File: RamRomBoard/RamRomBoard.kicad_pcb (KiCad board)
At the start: 2 copper layers, 100 x 100 mm, 74 parts, among them J1 BUS, J10 ., J13 ., J2 BUS, J3 Spare, J4 Spare, J5 Screw_Terminal_01x02, J6 USB_B_Micro, J7 STM32F401, J8 Dual LED Socket, J9 JTAG, SW1 033TBVSA, U1 74LVC125, U10 74AHC1G14, U11 IS61WV102416, U12 IS61WV10248EDBLL, U13 74LVC595, U14 74LVC595, U15 SN74LVC245ANSR, U16 SN74LVC245ANSR, U17 74LVC595, U18 74HC165, U19 SN74LVC245ANSR, U2 AZ1117-3.3, U3 74LVC08AD, U4 DS1085, U5 74LVC1G32, U6 74AHC1G14, U7 74HC590, U8 74HC590, U9 74HC590

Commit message: Readme update
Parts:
- J5: footprint Connector_Phoenix_MC:PhoenixContact_MCV_1,5_2-G-3.81_1x02_P3.81mm_Vertical -> TerminalBlock_RND:TerminalBlock_RND_205-00012_1x02_P5.00mm_Horizontal
- moved J5 0.67 mm to (61.2, 54.6)
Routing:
- net GND: track 979.5 -> 978.5 mm

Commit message: cpld examples update
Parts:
- U11: value IS61WV102416 -> IS61WV102416FBLL1T2
- U12: value IS61WV10248EDBLL -> IS61WV10248EDBLL-10TL
- U2: footprint Package_TO_SOT_SMD:SOT-89-3_Handsoldering -> Package_TO_SOT_SMD:SOT-223-3_TabPin2
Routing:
- net /A10: track 70.9 -> 68.1 mm
- net /A11: track 67.0 -> 64.9 mm
- net /A19: track 97.2 -> 95.2 mm
- net /A8: track 87.8 -> 85.9 mm
- net /A9: track 74.8 -> 73.4 mm
- net +5V: track 280.2 -> 278.9 mm
- net /A7: track 81.2 -> 80.2 mm
- net +3V3: track 716.5 -> 717.4 mm
- net /A14: track 64.5 -> 65.3 mm
- net /A6: track 87.9 -> 87.2 mm
- net /CPR: track 85.6 -> 85.0 mm
- net /A12: track 68.0 -> 67.5 mm

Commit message: New XC9572 Example
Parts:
- removed J10, J13: ., Connector_PinHeader_2.00mm:PinHeader_1x01_P2.00mm_Vertical
- added TP10: ., Connector_PinHeader_1.00mm:PinHeader_1x01_P1.00mm_Vertical, F.Cu at (80.3, 121.7)
- added TP11: ., Connector_PinHeader_1.00mm:PinHeader_1x01_P1.00mm_Vertical, F.Cu at (80.4, 113.9)
- added TP12: ., Connector_PinHeader_1.00mm:PinHeader_1x01_P1.00mm_Vertical, F.Cu at (58.4, 113.9)
- added TP13: ., Connector_PinHeader_1.00mm:PinHeader_1x01_P1.00mm_Vertical, F.Cu at (58.4, 119.1)
- added TP14: ., Connector_PinHeader_1.00mm:PinHeader_1x01_P1.00mm_Vertical, F.Cu at (58.5, 93.7)
- added TP15: ., Connector_PinHeader_1.00mm:PinHeader_1x01_P1.00mm_Vertical, F.Cu at (58.4, 103.9)
- R1: value 1k -> 560E
- moved REF** 83.6 mm to (62.2, 144.8), turned to 0 degrees
- moved REF** 76.3 mm to (76.8, 144.1), turned to 0 degrees
- moved C16 9.47 mm to (143.9, 121.3), turned to 0 degrees
- moved RN3 7.59 mm to (136.8, 131.6)
- moved RN4 7.59 mm to (138.0, 135.0)
- moved C13 6.30 mm to (131.2, 101.2)
- moved U10 6.30 mm to (116.5, 112.4)
- moved U15 6.30 mm to (132.0, 123.6)
- moved U16 6.30 mm to (118.7, 123.6)
- moved C10 6.30 mm to (110.1, 113.6)
- moved U13 6.30 mm to (130.7, 113.5)
- moved U14 6.30 mm to (117.5, 113.6)
- moved U11 6.21 mm to (131.8, 103.0)
- moved C11 0.55 mm to (124.1, 90.2)
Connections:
- net /uSCL renamed /uSCK
- net /uSDA renamed /uMOSI
- net /~{uSCL} renamed /~{uSCK}
- J2 pad 10: /Bus/RES1 -> /~{CE_EXT4}
- J2 pad 11: /Bus/RES0 -> /~{CE_EXT7}
- J2 pad 12: /~{CE_EXT0} -> /~{CE_EXT6}
- J2 pad 13: /~{CE_EXT1} -> /~{CE_EXT9}
- J2 pad 14: /~{CE_EXT2} -> /~{CE_EXT8}
- J2 pad 15: /~{CE_EXT3} -> /~{CE_EXT11}
- J2 pad 16: /~{CE_EXT4} -> /~{CE_EXT10}
- J2 pad 17: /~{CE_EXT5} -> /~{CE_EXT13}
- J2 pad 18: /~{CE_EXT6} -> /~{CE_EXT12}
- J2 pad 19: /~{CE_EXT7} -> /Bus/RES4
- J2 pad 20: /~{CE_EXT8} -> /Bus/RES5
- J2 pad 21: /~{CE_EXT9} -> /Bus/RES2
- J2 pad 22: /~{CE_EXT10} -> /Bus/RES3
- J2 pad 23: /~{CE_EXT11} -> /Bus/RES0
- J2 pad 24: /~{CE_EXT12} -> /Bus/RES1
- J2 pad 25: /~{CE_EXT13} -> /CLK1
- J2 pad 5: /Bus/RES6 -> /~{CE_EXT1}
- J2 pad 6: /Bus/RES5 -> /~{CE_EXT0}
- J2 pad 7: /Bus/RES4 -> /~{CE_EXT3}
- J2 pad 8: /Bus/RES3 -> /~{CE_EXT2}
- J2 pad 9: /Bus/RES2 -> /~{CE_EXT5}
- J4 pad 10: /Bus/RES1 -> /~{CE_EXT4}
- J4 pad 11: /Bus/RES0 -> /~{CE_EXT7}
- J4 pad 12: /~{CE_EXT0} -> /~{CE_EXT6}
- J4 pad 13: /~{CE_EXT1} -> /~{CE_EXT9}
- J4 pad 14: /~{CE_EXT2} -> /~{CE_EXT8}
- J4 pad 15: /~{CE_EXT3} -> /~{CE_EXT11}
- J4 pad 16: /~{CE_EXT4} -> /~{CE_EXT10}
- J4 pad 17: /~{CE_EXT5} -> /~{CE_EXT13}
- J4 pad 18: /~{CE_EXT6} -> /~{CE_EXT12}
- J4 pad 19: /~{CE_EXT7} -> /Bus/RES4
- J4 pad 20: /~{CE_EXT8} -> /Bus/RES5
- J4 pad 21: /~{CE_EXT9} -> /Bus/RES2
- J4 pad 22: /~{CE_EXT10} -> /Bus/RES3
- J4 pad 23: /~{CE_EXT11} -> /Bus/RES0
- J4 pad 24: /~{CE_EXT12} -> /Bus/RES1
- J4 pad 25: /~{CE_EXT13} -> /CLK1
- J4 pad 5: /Bus/RES6 -> /~{CE_EXT1}
- J4 pad 6: /Bus/RES5 -> /~{CE_EXT0}
- J4 pad 7: /Bus/RES4 -> /~{CE_EXT3}
- J4 pad 8: /Bus/RES3 -> /~{CE_EXT2}
- J4 pad 9: /Bus/RES2 -> /~{CE_EXT5}
- J7 pad 12: /B4 -> /CLK1#
- J7 pad 27: /SEL4 -> /uA1
- U1 pad 11: /CLKF -> /CLKS
- U1 pad 12: /CLKF# -> /CLKS#
- U1 pad 5: Net-(J10-Pin_1) -> /CLK1#
- U1 pad 6: Net-(J13-Pin_1) -> /CLK1
- U1 pad 8: /CLKS -> /CLKF
- U1 pad 9: /CLKS# -> /CLKF#
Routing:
- net GND: track 978.2 -> 934.7 mm, vias 22 -> 25
- net /CLK1: track 0.00 -> 41.8 mm
- net /CLK1#: track 0.00 -> 38.3 mm, vias 0 -> 1
- net +3V3: track 717.4 -> 726.6 mm, vias 45 -> 48
- net /~{CE_INT15}: track 56.8 -> 48.6 mm, vias 2 -> 1
- net /~{CE_INT0}: track 36.4 -> 28.7 mm
- net /~{CEDAT_EN}: track 72.1 -> 79.7 mm
- net /SDA: track 69.9 -> 62.4 mm
- net /uSCK: track 111.8 -> 118.9 mm
- net /Bus/RES6: track 7.03 -> 0.00 mm
- net /uMOSI: track 70.8 -> 77.4 mm
- net /~{CE_INT11}: track 13.0 -> 19.6 mm, vias 2 -> 1
- net /~{uSCK}: track 38.6 -> 44.8 mm
- net /A4: track 127.9 -> 122.0 mm
- net /A2: track 121.5 -> 115.5 mm
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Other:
- board text added: "GND x x 3V3 GND"

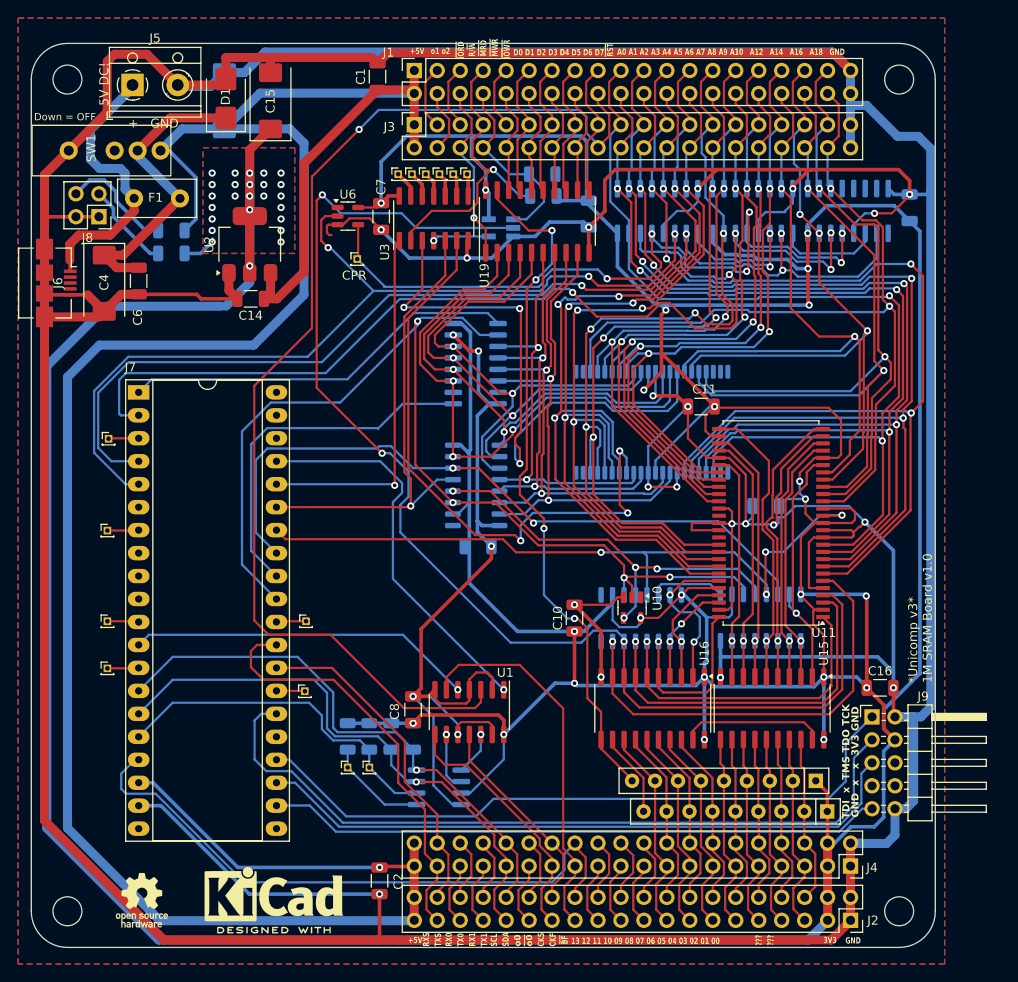
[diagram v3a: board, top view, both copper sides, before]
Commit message: Schematics of RAMROM Board updated
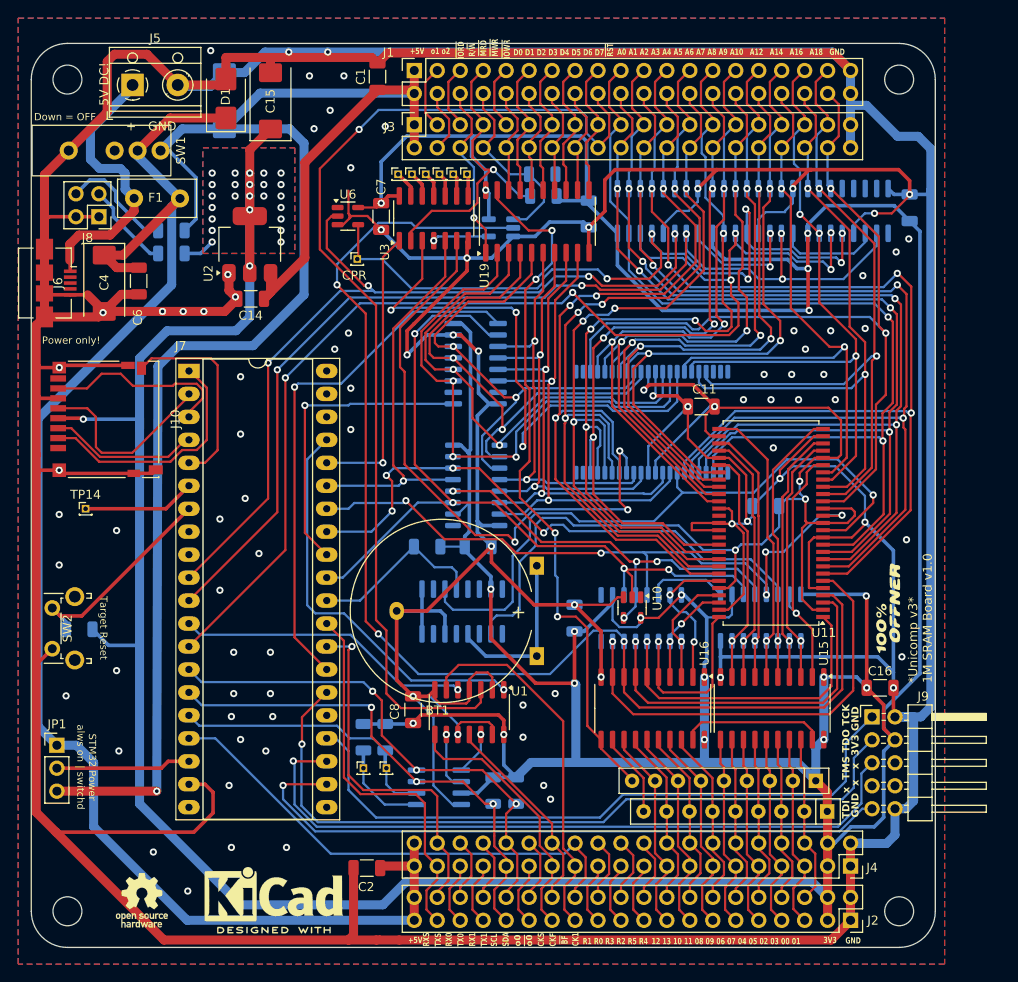
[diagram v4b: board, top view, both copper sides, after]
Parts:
- removed TP10, TP11, TP12, TP13, TP15: ., Connector_PinHeader_1.00mm:PinHeader_1x01_P1.00mm_Vertical
- added BT1: CR2032, my_own:Battery_CR2032_Horizontal_ThreeHoles, F.Cu at (105.9, 112.8)
- added G***: LOGO, my_own:Logo_100ProzentOffner_10x2.7mm, F.Cu at (144.8, 112.5)
- added J10: Micro_SD_Card_Det2, Connector_Card:microSD_HC_Hirose_DM3D-SF, F.Cu at (58.3, 91.6)
- added JP1: VSEL, Connector_PinHeader_2.54mm:PinHeader_1x03_P2.54mm_Vertical, F.Cu at (52.8, 127.6)
- added R10: 10k, Resistor_SMD:R_1206_3216Metric, B.Cu at (55.3, 114.8)
- added R9: 10k, Resistor_SMD:R_1206_3216Metric, B.Cu at (93.8, 105.7)
- added SW2: SW_Push, Button_Switch_THT:SW_Tactile_SPST_Angled_PTS645Vx31-2LFS, F.Cu at (52.3, 117.0)
- added U20: DS1314, Package_SO:SOIC-16_3.9x9.9mm_P1.27mm, B.Cu at (97.7, 112.8)
- C10: moved to B.Cu
- moved R3 12.9 mm to (103.6, 132.6)
- moved R4 12.8 mm to (101.1, 132.6)
- moved TP14 8.15 mm to (56.0, 101.5)
- moved J7 6.04 mm to (67.4, 86.2)
- moved C2 1.98 mm to (87.1, 141.2), turned to 180 degrees
- moved TP9 1.88 mm to (89.3, 130.2)
- moved R6 1.77 mm to (89.2, 126.7)
- moved R5 1.74 mm to (86.7, 126.7)
- moved TP8 1.74 mm to (86.7, 130.2)
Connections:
- C11 pad 1: +3V3 -> VCCQ
- C13 pad 1: +3V3 -> VCCQ
- C2 pad 1: +5V -> +5VA
- C4 pad 1: Net-(D1-K) -> +5VA
- C6 pad 1: Net-(D1-K) -> +5VA
- D1 pad 1: Net-(D1-K) -> +5VA
- F1 pad 2: Net-(D1-K) -> +5VA
- J2 pad 39: +5V -> +5VA
- J2 pad 40: +5V -> +5VA
- J4 pad 39: +5V -> +5VA
- J4 pad 40: +5V -> +5VA
- J7 pad 1: /~{PLD} -> /~{CS_SD}
- J7 pad 10: /~{uMRD} -> /CNT
- J7 pad 11: /B3 -> /~{MRC}
- J7 pad 13: /B5 -> /~{CNTOE}
- J7 pad 18: +5V -> Net-(J7-Pin_18)
- J7 pad 2: /~{CNTOE} -> /SCK_SD
- J7 pad 27: /uA1 -> /~{PLD}
- J7 pad 3: /B14 -> /MISO_SD
- J7 pad 30: /uA4 -> /~{BW}
- J7 pad 4: /~{MRC} -> /MOSI_SD
- J7 pad 5: /CNT -> /DET_SD
- J7 pad 6: /~{uMWR} -> /uA9
- J7 pad 7: /uA10 -> /~{EXTRST}
- SW1 pad 2: Net-(D1-K) -> +5VA
- TP14 pad 1: /B14 -> /uA9
- U11 pad 13: GND -> /~{RAMCE}
- U11 pad 14: +3V3 -> VCCQ
- U11 pad 16: +3V3 -> VCCQ
- U11 pad 2: +3V3 -> VCCQ
- U11 pad 23: +3V3 -> VCCQ
- U11 pad 29: +3V3 -> VCCQ
- U11 pad 50: +3V3 -> VCCQ
- U12 pad 11: +3V3 -> VCCQ
- U12 pad 33: +3V3 -> VCCQ
- U12 pad 8: GND -> /~{RAMCE}
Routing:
- net +5VA: track 0.00 -> 166.1 mm
- net VCCQ: track 0.00 -> 133.5 mm, vias 0 -> 5
- net +5V: track 278.9 -> 190.1 mm
- net +3V3: track 726.6 -> 641.7 mm, vias 48 -> 44
- net /~{RAMCE}: track 0.00 -> 72.8 mm, vias 0 -> 1
- net GND: track 934.7 -> 1003.9 mm, vias 25 -> 89
- net Net-(D1-K): track 34.0 -> 0.00 mm
- net /~{CS_SD}: track 0.00 -> 27.1 mm
- net /uSCK: track 118.9 -> 92.3 mm
- net /~{EXTRST}: track 0.00 -> 23.4 mm
- net /DET_SD: track 0.00 -> 22.3 mm
- net /SCK_SD: track 0.00 -> 21.3 mm
- net /MISO_SD: track 0.00 -> 21.2 mm
- net /~{BW}: track 0.00 -> 19.9 mm
- net Net-(BT1-+): track 0.00 -> 18.9 mm
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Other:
- board text added: "12 13 10 11 08 09 06 07 04 05 02 03 00 01"
- board text added: "CK1"
- board text added: "Connector J1 and J2 3mm from Edge. Conn. J3 and J4 9mm from Edge."
- board text added: "Power only!"
- board text added: "R1 R0 R3 R2 R5 R4"
- board text added: "STM32 Power alws on | switchd"
- board text added: "Target Reset"
- board text removed: "13 12 11 10 09 08 07 06 05 04 03 02 01 00"
- board text removed: "???"
- board text removed: "Connector J1 and J3 3mm from Edge."

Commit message: Diodes on Databus added, DS1314 different footprint
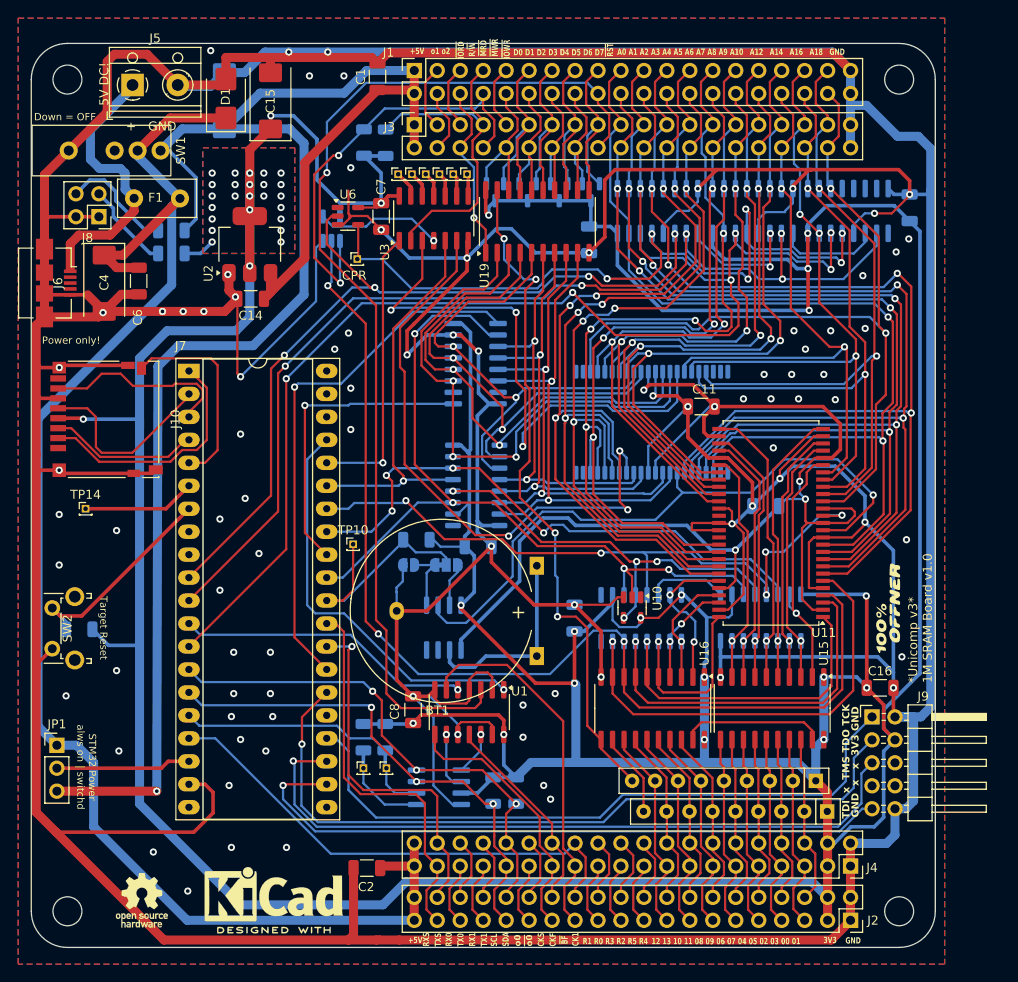
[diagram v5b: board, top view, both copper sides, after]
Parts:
- added D2: BAV70, Package_TO_SOT_SMD:SOT-23, B.Cu at (104.9, 66.5)
- added D3: BAV70, Package_TO_SOT_SMD:SOT-23, B.Cu at (101.3, 66.5)
- added D4: BAV70, Package_TO_SOT_SMD:SOT-23, B.Cu at (108.4, 66.5)
- added D5: BAV70, Package_TO_SOT_SMD:SOT-23, B.Cu at (111.9, 66.5)
- added JP2: MODE1, Jumper:SolderJumper-3_P1.3mm_Bridged12_RoundedPad1.0x1.5mm, B.Cu at (95.9, 107.7)
- added JP3: MODE2, Jumper:SolderJumper-2_P1.3mm_Open_RoundedPad1.0x1.5mm, B.Cu at (91.8, 107.7)
- added TP10: ., Connector_PinHeader_1.00mm:PinHeader_1x01_P1.00mm_Vertical, F.Cu at (85.6, 105.4)
- U20: footprint Package_SO:SOIC-16_3.9x9.9mm_P1.27mm -> Package_SO:SOIC-8_3.9x4.9mm_P1.27mm
- moved R7 20.0 mm to (86.8, 61.0), turned to 90 degrees
- moved U5 18.8 mm to (83.2, 70.5), turned to 90 degrees
- moved R8 18.4 mm to (89.2, 61.0), turned to 90 degrees
- moved C5 2.86 mm to (111.7, 71.7)
- moved U20 2.70 mm to (95.6, 114.6)
- moved R9 1.42 mm to (92.6, 104.9)
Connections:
- U20 pad 1: unconnected-(U20-Pad1) -> VCCQ
- U20 pad 2: VCCQ -> Net-(BT1-+)
- U20 pad 3: unconnected-(U20-Pad3) -> GND
- U20 pad 4: Net-(BT1-+) -> (no net)
- U20 pad 5: unconnected-(U20-Pad5) -> Net-(JP2-A)
- U20 pad 6: GND -> /~{RAMCE}
- U20 pad 7: unconnected-(U20-Pad7) -> Net-(JP2-B)
- U20 pad 8: GND -> +3V3
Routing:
- net /~{MWR}: track 21.3 -> 47.9 mm, vias 0 -> 2
- net GND: track 1003.9 -> 1029.8 mm, vias 89 -> 86
- net /~{CE_INT14}: track 139.5 -> 120.9 mm
- net Net-(U3-Pad4): track 6.28 -> 14.1 mm
- net /D1: track 15.0 -> 22.7 mm
- net /D7: track 15.0 -> 22.6 mm
- net /D3: track 15.0 -> 22.3 mm
- net /D5: track 15.0 -> 22.2 mm
- net Net-(JP2-A): track 0.00 -> 7.01 mm
- net /~{BW}: track 19.9 -> 26.2 mm
- net /D0: track 11.7 -> 16.5 mm
- net Net-(JP2-B): track 0.00 -> 4.84 mm
- net /~{MRD}: track 33.6 -> 38.1 mm, vias 1 -> 0
- net /D2: track 11.9 -> 16.3 mm
- net /D6: track 12.0 -> 16.4 mm
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
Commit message: many new boards
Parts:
- removed REF**: KiCad-Logo2_6mm_SilkScreen, Symbol:KiCad-Logo2_6mm_SilkScreen
- removed REF**: OSHW-Logo_5.7x6mm_SilkScreen, Symbol:OSHW-Logo_5.7x6mm_SilkScreen
- added D10: BAV70, Package_TO_SOT_SMD:SOT-23, F.Cu at (125.4, 78.2)
- added D11: BAV70, Package_TO_SOT_SMD:SOT-23, F.Cu at (121.8, 78.3)
- added D6: BAV70, Package_TO_SOT_SMD:SOT-23, F.Cu at (139.6, 78.2)
- added D7: BAV70, Package_TO_SOT_SMD:SOT-23, F.Cu at (135.9, 78.2)
- added D8: BAV70, Package_TO_SOT_SMD:SOT-23, F.Cu at (132.4, 78.3)
- added D9: BAV70, Package_TO_SOT_SMD:SOT-23, F.Cu at (128.9, 78.2)
- added JP4: ~{CE_INT14} / ~{CE_EXT14}, Jumper:SolderJumper-3_P1.3mm_Bridged12_RoundedPad1.0x1.5mm, B.Cu at (115.6, 123.4)
- added JP5: RD_Ovr, Jumper:SolderJumper-2_P1.3mm_Open_RoundedPad1.0x1.5mm, F.Cu at (92.5, 74.8)
- added JP6: U3_Ovr, Jumper:SolderJumper-2_P1.3mm_Open_RoundedPad1.0x1.5mm, F.Cu at (96.0, 74.8)
- added JP7: WR_Ovr, Jumper:SolderJumper-2_P1.3mm_Open_RoundedPad1.0x1.5mm, B.Cu at (86.5, 75.1)
- added TP11: ~{CEin}, Connector_PinHeader_1.00mm:PinHeader_1x01_P1.00mm_Vertical, F.Cu at (110.7, 131.3)
- D2, D3, D4, D5: moved to F.Cu
- JP2: value MODE1 -> ~{CEi} or ~{BW}
- JP3: value MODE2 -> ~{CEi} to GND
- TP10: value . -> ~{BW}; moved to B.Cu
- TP7: moved to B.Cu
- moved D3 46.3 mm to (145.8, 79.1), turned to 0 degrees
- moved D2 42.4 mm to (146.4, 75.2), turned to 0 degrees
- moved D4 40.1 mm to (145.2, 82.5), turned to 0 degrees
- moved D5 37.6 mm to (143.9, 86.1), turned to 0 degrees
- moved TP7 1.87 mm to (86.3, 72.0), turned to 180 degrees
- moved J9 1.46 mm to (144.5, 124.5)
- turned TP10 to 180 degrees
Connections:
- net /Bus/RES1 renamed /RES1
- net /Bus/RES2 renamed /RES2
- net /Bus/RES3 renamed /RES3
- net /Bus/RES4 renamed /RES4
- net /Bus/RES5 renamed /RES5
- net /Bus/RX0 renamed /RX0
- net /Bus/RX1 renamed /RX1
- net /Bus/TX0 renamed /TX0
- net /Bus/TX1 renamed /TX1
- D2 pad 1: /D2 -> /A4
- D2 pad 2: /D3 -> /A3
- D3 pad 1: /D0 -> /A2
- D3 pad 2: /D1 -> /A1
- D4 pad 1: /D4 -> /A0
- D4 pad 2: /D5 -> /A19
- D5 pad 1: /D6 -> /A18
- D5 pad 2: /D7 -> /A17
- J2 pad 23: /Bus/RES0 -> /~{STM32BUS}
- J4 pad 23: /Bus/RES0 -> /~{STM32BUS}
- J7 pad 6: /uA9 -> /~{STM32BUS}
- TP14 pad 1: /uA9 -> /~{STM32BUS}
- U20 pad 4: (no net) -> GND
- U5 pad 2: /~{CE_INT14} -> Net-(JP4-C)
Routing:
- net /~{STM32BUS}: track 0.00 -> 101.5 mm
- net Net-(JP4-C): track 0.00 -> 81.5 mm, vias 0 -> 2
- net /~{CE_INT14}: track 120.9 -> 49.2 mm, vias 3 -> 1
- net GND: track 1029.8 -> 1072.5 mm, vias 86 -> 101
- net Net-(JP2-A): track 7.01 -> 36.4 mm, vias 0 -> 1
- net +3V3: track 639.8 -> 667.8 mm, vias 45 -> 55
- net /~{CNTOE}: track 131.5 -> 114.7 mm, vias 6 -> 3
- net /uA9: track 12.5 -> 0.00 mm
- net /CPR: track 86.7 -> 74.7 mm, vias 6 -> 2
- net /~{MRAM_WR}: track 43.7 -> 54.9 mm, vias 1 -> 3
- net Net-(JP6-B): track 14.1 -> 23.3 mm
- net /D1: track 22.7 -> 15.0 mm
- net /D7: track 22.6 -> 15.0 mm
- net /D3: track 22.3 -> 15.0 mm
- net /D5: track 22.2 -> 15.0 mm
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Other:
- board text added: "JTAG Connector @ 144.46/124.5"
- board text added: "TDI x TMS TDO TCK GND x x 3V3 GND"
- board text removed: "CPR"
- board text removed: "GND x x 3V3 GND"
- board text removed: "TDI x TMS TDO TCK"
